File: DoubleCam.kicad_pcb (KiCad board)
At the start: 2 copper layers, 68 x 43.3 mm, 26 parts, among them J1 Conn_01x24_MountingPin, J2 Conn_01x24_MountingPin, J3 Conn_02x20_Odd_Even, U1 XC6206PxxxMR, U2 XC6206PxxxMR, X1 SG-3225CAN

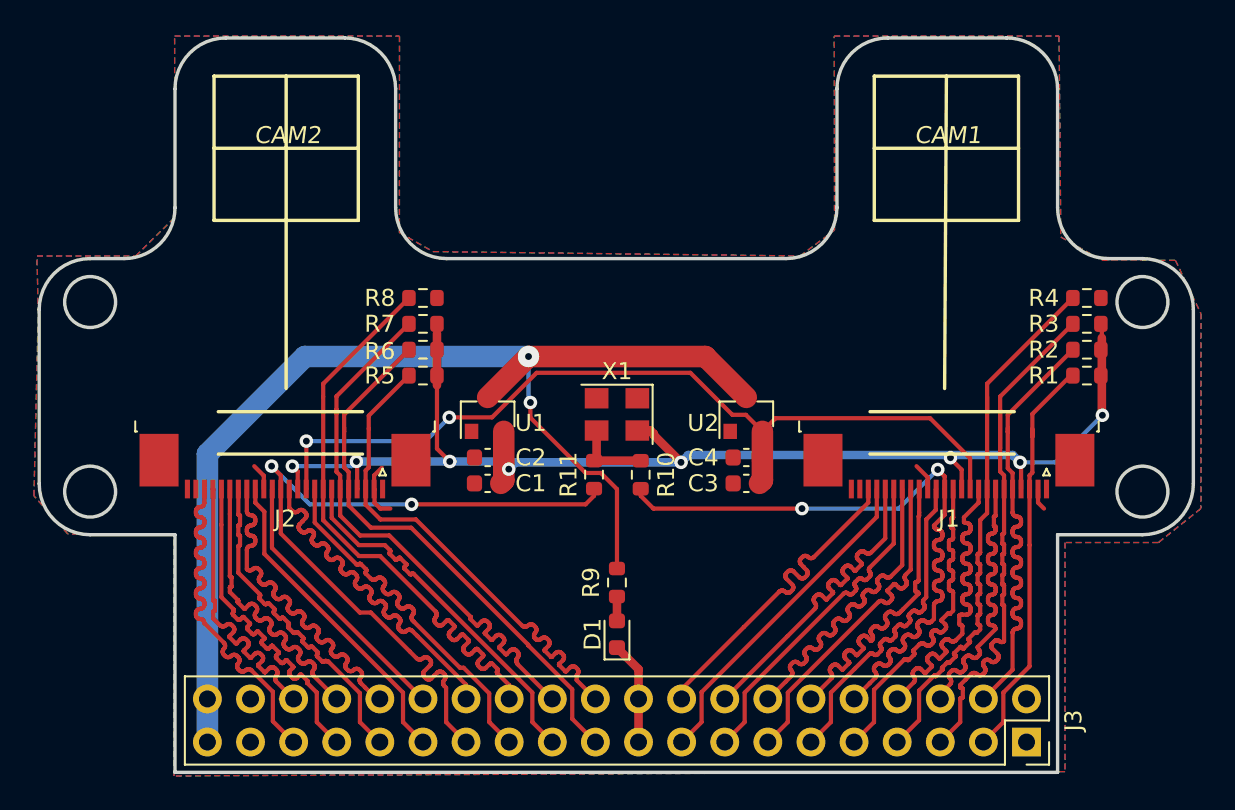
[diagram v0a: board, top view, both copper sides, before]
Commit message: changed FPC connect
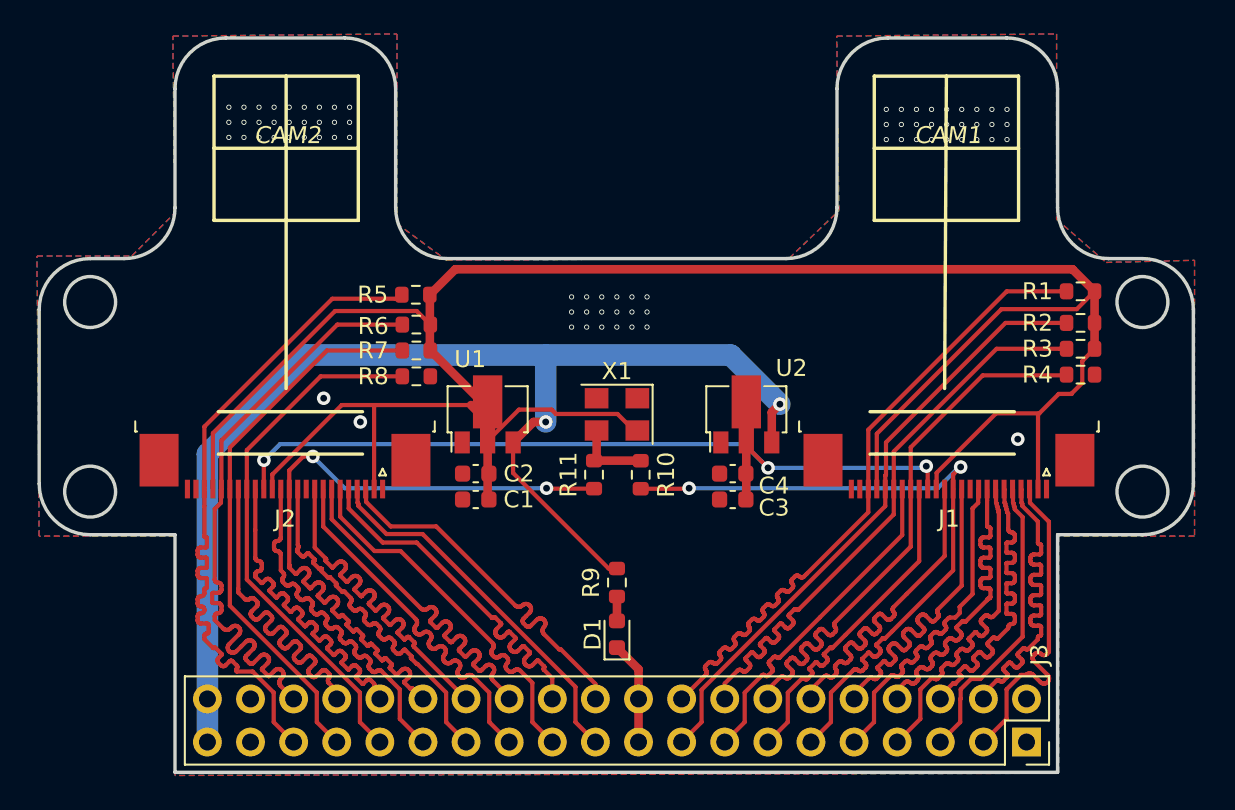
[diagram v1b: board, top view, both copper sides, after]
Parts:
- U1, U2: footprint Package_TO_SOT_SMD:SOT-23 -> Package_TO_SOT_SMD:SOT-89-3
- moved R1 4.98 mm to (192.4, 69.0)
- moved R5 4.78 mm to (153.2, 69.2)
- moved R8 4.63 mm to (153.3, 74.0)
- moved R4 4.53 mm to (192.4, 73.9)
- moved R2 1.62 mm to (192.4, 70.8)
- moved R7 1.62 mm to (153.3, 72.4)
- moved R6 1.53 mm to (153.3, 70.9)
- moved R3 1.51 mm to (192.4, 72.3)
- moved C3 1.24 mm to (171.9, 81.2)
- moved C4 1.24 mm to (171.9, 79.7)
- moved C1 1.18 mm to (156.8, 81.2)
- moved C2 1.18 mm to (156.8, 79.7)
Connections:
- net +5V renamed Net-(J3-Pad2)
- J1 pad 1: Net-(J1-Pad1) -> GND
- J1 pad 10: +1V5 -> GND
- J1 pad 11: +2V8 -> /OV1_D6
- J1 pad 12: /OV1_D7 -> /OV1_XCLK
- J1 pad 13: /OV1_XCLK -> /OV1_D7
- J1 pad 14: /OV1_D6 -> +2V8
- J1 pad 15: GND -> +1V5
- J1 pad 16: /OV1_D5 -> /OV1_HREF
- J1 pad 17: /OV1_PCLK -> /OV1_PWDN
- J1 pad 18: /OV1_D4 -> /OV1_VSYNC
- J1 pad 19: /OV1_D0 -> /OV1_RESET
- J1 pad 2: GND -> +2V8
- J1 pad 20: /OV1_D3 -> /OV1_SCL
- J1 pad 21: /OV1_D1 -> +2V8
- J1 pad 22: /OV1_D2 -> /OV1_SDA
- J1 pad 23: Net-(J1-Pad23) -> GND
- J1 pad 3: /OV1_SDA -> /OV1_D2
- J1 pad 4: +2V8 -> /OV1_D1
- J1 pad 5: /OV1_SCL -> /OV1_D3
- J1 pad 6: /OV1_RESET -> /OV1_D0
- J1 pad 7: /OV1_VSYNC -> /OV1_D4
- J1 pad 8: /OV1_PWDN -> /OV1_PCLK
- J1 pad 9: /OV1_HREF -> /OV1_D5
- J2 pad 1: Net-(J2-Pad1) -> GND
- J2 pad 10: +1V5 -> GND
- J2 pad 11: +2V8 -> /OV2_D6
- J2 pad 12: /OV2_D7 -> /OV2_XCLK
- J2 pad 13: /OV2_XCLK -> /OV2_D7
- J2 pad 14: /OV2_D6 -> +2V8
- J2 pad 15: GND -> +1V5
- J2 pad 16: /OV2_D5 -> /OV2_HREF
- J2 pad 17: /OV2_PCLK -> /OV2_PWDN
- J2 pad 18: /OV2_D4 -> /OV2_VSYNC
- J2 pad 19: /OV2_D0 -> /OV2_RESET
- J2 pad 2: GND -> +2V8
- J2 pad 20: /OV2_D3 -> /OV2_SCL
- J2 pad 21: /OV2_D1 -> +2V8
- J2 pad 22: /OV2_D2 -> /OV2_SDA
- J2 pad 23: Net-(J2-Pad23) -> GND
- J2 pad 3: /OV2_SDA -> /OV2_D2
- J2 pad 4: +2V8 -> /OV2_D1
- J2 pad 5: /OV2_SCL -> /OV2_D3
- J2 pad 6: /OV2_RESET -> /OV2_D0
- J2 pad 7: /OV2_VSYNC -> /OV2_D4
- J2 pad 8: /OV2_PWDN -> /OV2_PCLK
- J2 pad 9: /OV2_HREF -> /OV2_D5
- J3 pad 1: GND -> Net-(J3-Pad1)
- J3 pad 10: /OV1_XCLK -> /OV1_D6
- J3 pad 11: /OV1_D6 -> /OV1_XCLK
- J3 pad 12: /OV1_D5 -> /OV1_D7
- J3 pad 13: /OV1_PCLK -> /OV1_HREF
- J3 pad 14: /OV1_D4 -> /OV1_PWDN
- J3 pad 15: /OV1_D0 -> /OV1_VSYNC
- J3 pad 16: /OV1_D3 -> /OV1_RESET
- J3 pad 17: /OV1_D1 -> /OV1_SCL
- J3 pad 18: /OV1_D2 -> /OV1_SDA
- J3 pad 21: /OV2_SCL -> /OV2_D1
- J3 pad 22: /OV2_SDA -> /OV2_D2
- J3 pad 23: /OV2_VSYNC -> /OV2_D0
- J3 pad 24: /OV2_RESET -> /OV2_D3
- J3 pad 25: /OV2_HREF -> /OV2_PCLK
- J3 pad 26: /OV2_PWDN -> /OV2_D4
- J3 pad 27: /OV2_XCLK -> /OV2_D6
- J3 pad 28: /OV2_D7 -> /OV2_D5
- J3 pad 29: /OV2_D5 -> /OV2_D7
- J3 pad 3: /OV1_SDA -> /OV1_D2
- J3 pad 30: /OV2_D6 -> /OV2_XCLK
- J3 pad 31: /OV2_D4 -> /OV2_PWDN
- J3 pad 32: /OV2_PCLK -> /OV2_HREF
- J3 pad 33: /OV2_D3 -> /OV2_RESET
- J3 pad 34: /OV2_D0 -> /OV2_VSYNC
- J3 pad 35: /OV2_D2 -> /OV2_SDA
- J3 pad 36: /OV2_D1 -> /OV2_SCL
- J3 pad 4: /OV1_SCL -> /OV1_D1
- J3 pad 5: /OV1_RESET -> /OV1_D3
- J3 pad 6: /OV1_VSYNC -> /OV1_D0
- J3 pad 7: /OV1_PWDN -> /OV1_D4
- J3 pad 8: /OV1_HREF -> /OV1_PCLK
- J3 pad 9: /OV1_D7 -> /OV1_D5
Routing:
- net +2V8: track 76.5 -> 146.2 mm, vias 8 -> 0
- net /OV1_SDA: track 24.3 -> 38.7 mm
- net /OV2_SDA: track 29.9 -> 40.4 mm
- net /OV1_SCL: track 26.6 -> 36.2 mm
- net GND: track 13.9 -> 6.09 mm, vias 0 -> 75
- net /OV2_D6: track 16.1 -> 22.0 mm
- net /OV2_SCL: track 32.5 -> 38.3 mm
- net /OV2_D0: track 18.2 -> 22.1 mm
- net /OV2_PWDN: track 35.1 -> 31.4 mm
- net /OV2_D1: track 18.6 -> 22.0 mm
- net /OV2_D5: track 19.0 -> 22.0 mm
- net +3V3: track 70.7 -> 73.4 mm
- net +1V5: track 51.3 -> 48.7 mm, vias 2 -> 3
- net /OV1_VSYNC: track 17.6 -> 20.0 mm
- net /OV2_D4: track 19.8 -> 22.1 mm
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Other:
- net class OV1 added: clearance 0.2, trace_width 0.25, via_dia 0.8, via_drill 0.4
- net class OV2 added: clearance 0.2, trace_width 0.25, via_dia 0.8, via_drill 0.4
- rule via_min_size: 0.4 -> 0.1778
- board text added: "NC"
- board text removed: "V5.0"

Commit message: 修改等长线
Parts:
- moved R1 14.9 mm to (178.4, 74.1), turned to 0 degrees
- moved R4 14.8 mm to (178.4, 69.1), turned to 180 degrees
- moved R3 14.1 mm to (178.4, 70.7), turned to 0 degrees
- moved R2 14.1 mm to (178.4, 72.2), turned to 0 degrees
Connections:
- J3 pad 19: GND -> (no net)
- J3 pad 20: GND -> (no net)
- U1 pad 2: +2V8 -> +3V3
- U1 pad 3: +3V3 -> +2V8
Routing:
- net +2V8: track 146.2 -> 130.5 mm
- net /OV1_SDA: track 38.7 -> 24.0 mm
- net /OV2_SCL: track 38.3 -> 30.5 mm
- net /OV1_RESET: track 34.8 -> 27.6 mm
- net /OV2_VSYNC: track 21.9 -> 14.8 mm
- net /OV1_SCL: track 36.2 -> 29.2 mm
- net /OV1_D1: track 19.9 -> 13.3 mm
- net /OV2_HREF: track 22.0 -> 15.4 mm
- net /OV2_XCLK: track 41.9 -> 35.8 mm
- net /OV1_D0: track 20.0 -> 13.9 mm
- net /OV2_D5: track 22.0 -> 16.1 mm
- net /OV2_D4: track 22.1 -> 16.7 mm
- net /OV1_PCLK: track 19.9 -> 14.6 mm
- net /OV1_D6: track 19.9 -> 15.0 mm
- net /OV2_SDA: track 40.4 -> 35.5 mm
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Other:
- board text added: "2021.03.08"
- board text removed: "2020.11.26"
